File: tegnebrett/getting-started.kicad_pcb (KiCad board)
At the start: 2 copper layers, 11 parts, among them J1 FH12-45S-0.5SH55, J2 FH12-6S-1SH55, J3 Conn_ST_STDC14, J4 DA15_Socket, J5 MCU_Header_Pin, J6 FPGA_Header_Pin, J8 USB-A1HSW6, U2 Oscillator 100MHz, U5 STM32U5G7VJTxQ, U6 VGA Transceiver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

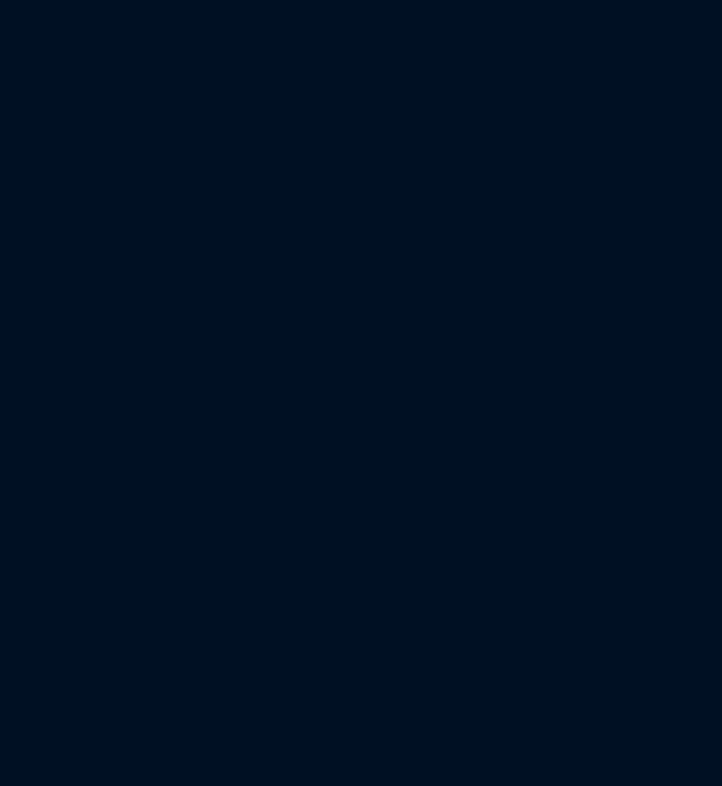
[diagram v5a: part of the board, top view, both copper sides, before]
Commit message: feat: add power supply component footprint
Also add to PCB.
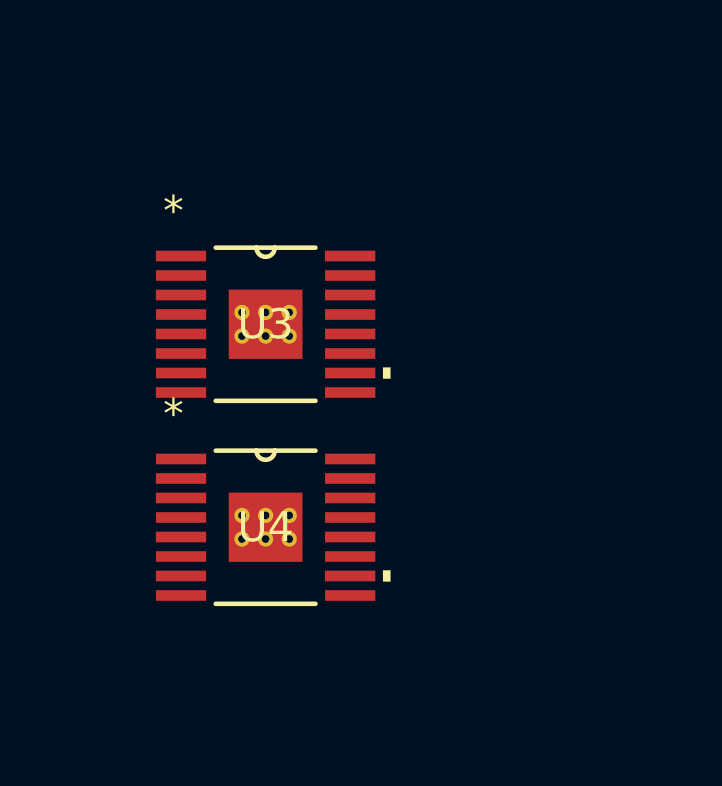
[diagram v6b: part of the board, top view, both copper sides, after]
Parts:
- added U3: TPS54294PWP1, tegnebrett_modules:PWP16_2P31X2P46, F.Cu at (20.2, 102.5)
- added U4: TPS54294PWP2, tegnebrett_modules:PWP16_2P31X2P46, F.Cu at (20.2, 109.2)

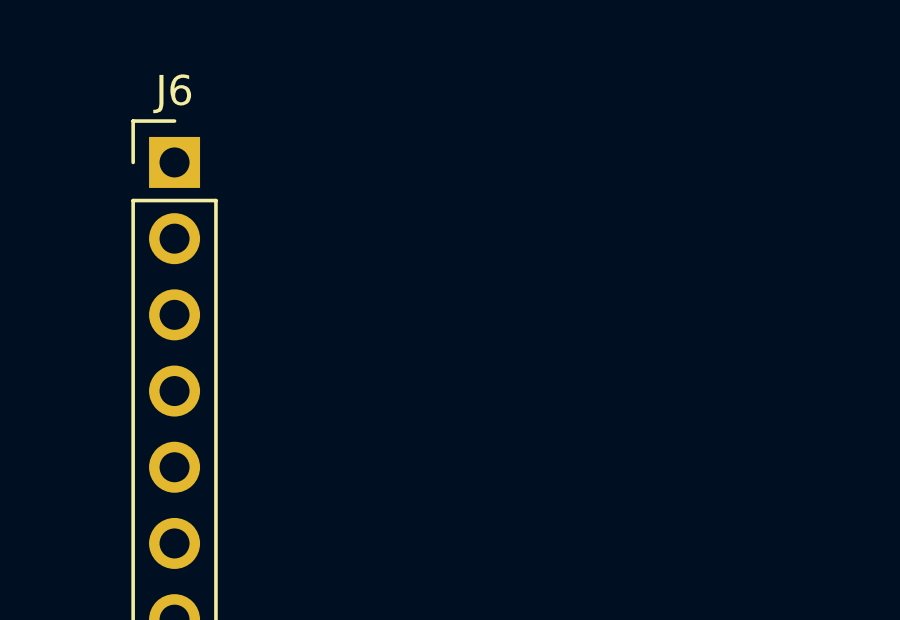
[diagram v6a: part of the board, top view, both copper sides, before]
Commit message: feat: add psram footprint and add to PCB
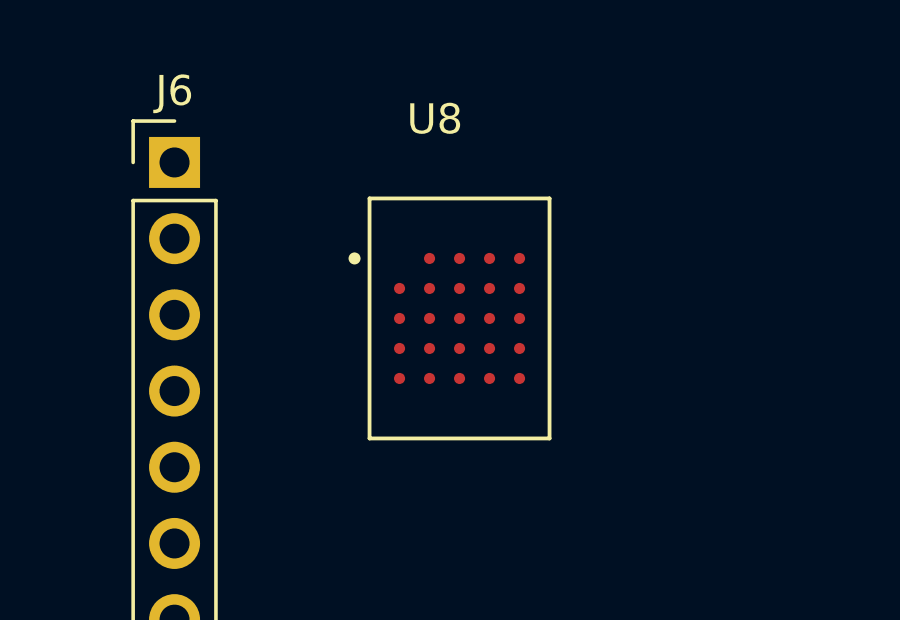
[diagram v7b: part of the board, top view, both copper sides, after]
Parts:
- added U8: IS66WVH16M8DBLL-100B1LI1, tegnebrett_modules:psram, F.Cu at (43.0, 21.5)

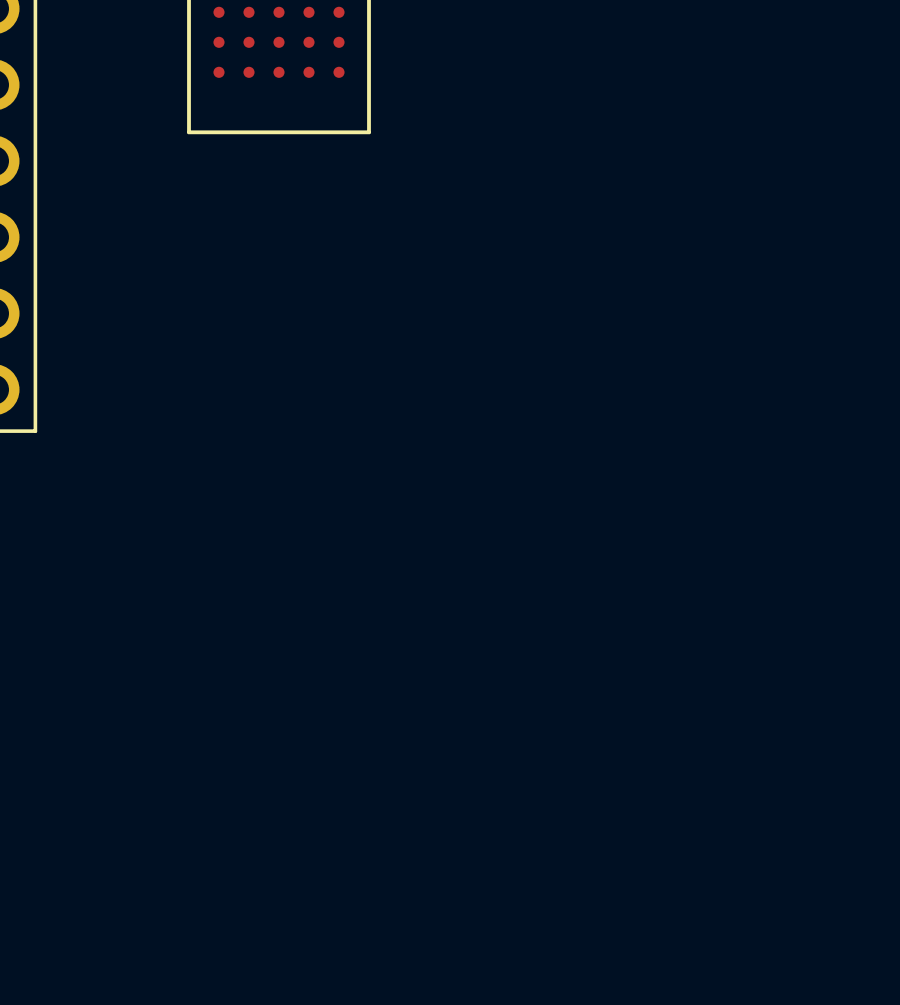
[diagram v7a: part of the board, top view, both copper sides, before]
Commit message: feat: add FPGA footprint and add footprint to PCB
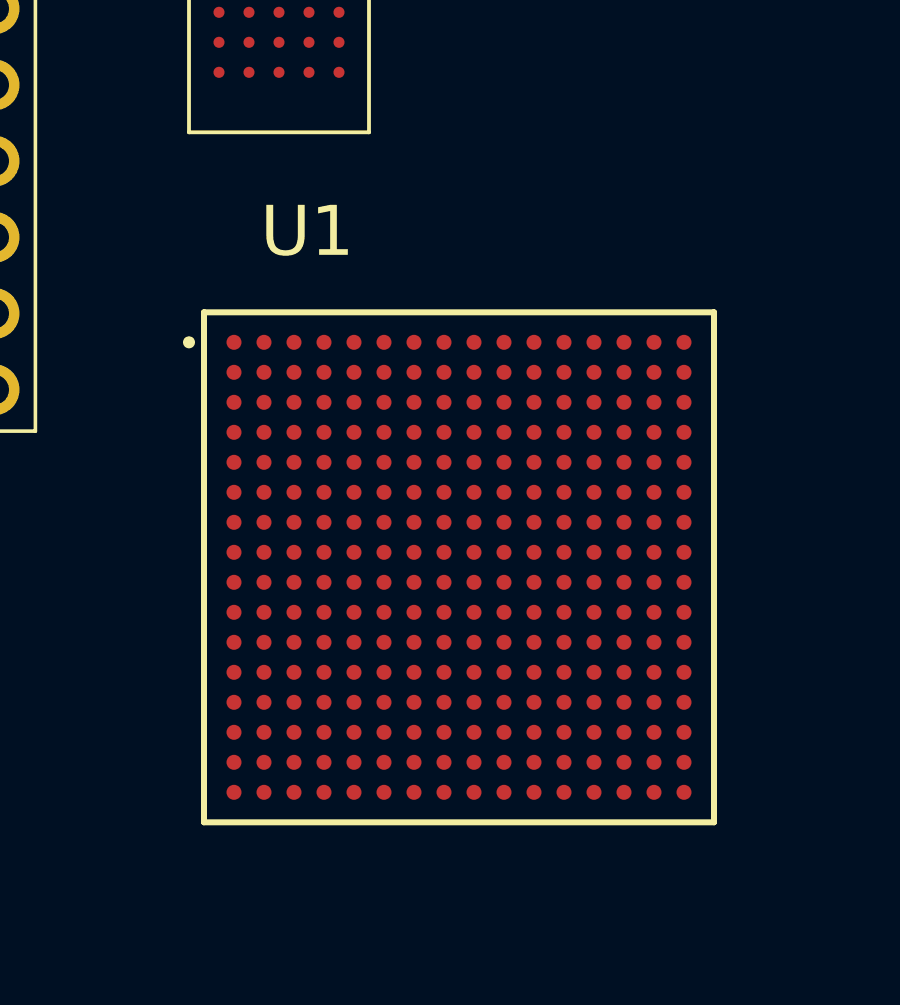
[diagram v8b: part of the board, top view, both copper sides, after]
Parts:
- added U1: XC7A100T-2FTG256I, tegnebrett_modules:fpga, F.Cu at (49.0, 40.0)
